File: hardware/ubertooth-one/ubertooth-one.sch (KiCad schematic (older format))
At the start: 88 parts, among them J1 USB-DEVICE, P1 SMA-CONN, P10 ATEST1, P11 ATEST2, P12 DCLK, P13 DIO, P2 PROGRAM, P3 JTAG, P4 EXPAND, P5 1V8, P6 3V3, P7 VBUS, P8 GIO1, P9 GIO6, Q1 BC856, U1 CC2591, U3 CC2400, U4 LPC175X, U6 IP4220CZ6, U7 TPS71219, X1 ABMM2

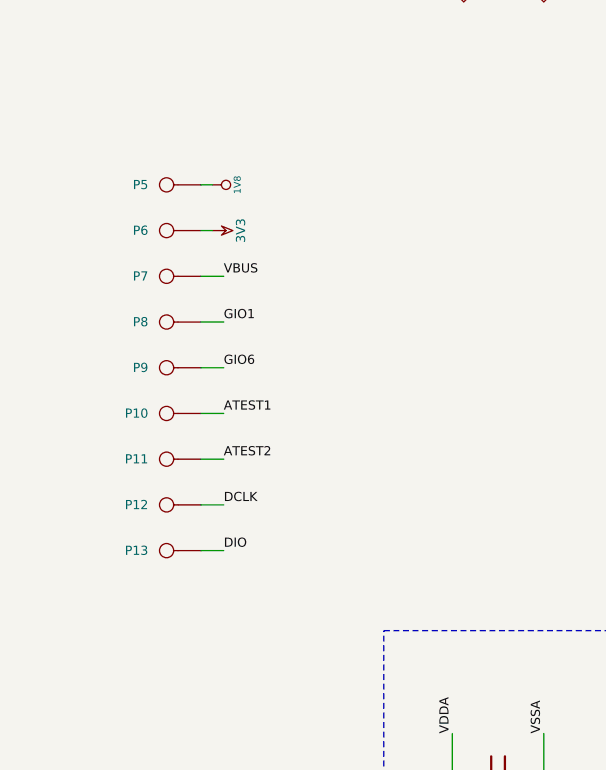
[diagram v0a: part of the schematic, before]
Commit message: added DNP fields
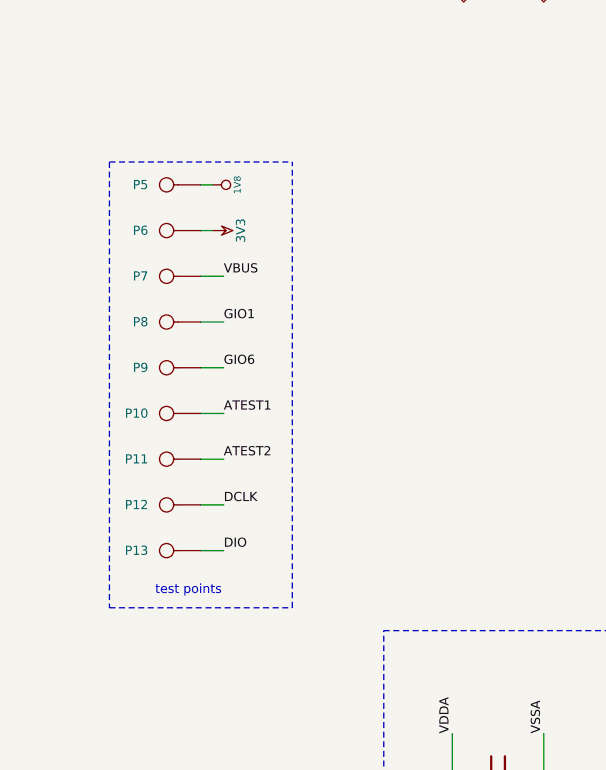
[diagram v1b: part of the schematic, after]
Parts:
- C10, C11, C8, FB1, FB2, FB3, FB4, L3, P2, P3, P4: Field3 (none) -> DNP
- C19, C21: footprint 0402 -> 0603
- C7: Field1 (none) -> foo; Field3 (none) -> DNP
- J1: footprint USB-A-MOLEX-480371000 -> USB-A-USAM-04
- P10, P11, P12, P13, P5, P6, P7, P8, P9: footprint (none) -> testpad-30mil; Field3 (none) -> DNP
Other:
- note added: "test points"

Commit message: rearranged regulator section with 0603s for ease of assembly
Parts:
- C35, C36, R18, R19: footprint 0402 -> 0603
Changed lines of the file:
@@
-EESchema Schematic File Version 2  date Sun Mar 20 08:07:46 2011
+EESchema Schematic File Version 2  date Sun Mar 20 10:47:56 2011
 LIBS:ubertooth-symbols
 LIBS:power
@@
 F 0 "C36" H 7250 7700 50  0000 L CNN
 F 1 "15pF" H 7250 7500 50  0000 L CNN
-F 2 "0402" H 7200 7600 60  0001 C CNN
+F 2 "0603" H 7200 7600 60  0001 C CNN
 F 4 "Murata" H 7200 7600 60  0001 C CNN "Field1"
 F 5 "GRM1535C1H150JDD5D" H 7200 7600 60  0001 C CNN "Field2"
@@
 F 0 "C35" H 6600 7750 50  0000 L CNN
 F 1 "10nF" H 6600 7550 50  0000 L CNN
-F 2 "0402" H 6550 7650 60  0001 C CNN
+F 2 "0603" H 6550 7650 60  0001 C CNN
 F 4 "Murata" H 6550 7650 60  0001 C CNN "Field1"
 F 5 "GRM155R71E103KA01D" H 6550 7650 60  0001 C CNN "Field2"
@@
 F 0 "R19" V 7030 8250 50  0000 C CNN
 F 1 "30.1k" V 6950 8250 50  0000 C CNN
-F 2 "0402" H 6950 8250 60  0001 C CNN
+F 2 "0603" H 6950 8250 60  0001 C CNN
 F 4 "KOA Speer" H 6950 8250 60  0001 C CNN "Field1"
 F 5 "RK73H1ETTP3012F" H 6950 8250 60  0001 C CNN "Field2"
@@
 F 0 "R18" V 7030 7550 50  0000 C CNN
 F 1 "49.9k" V 6950 7550 50  0000 C CNN
-F 2 "0402" H 6950 7550 60  0001 C CNN
+F 2 "0603" H 6950 7550 60  0001 C CNN
 F 4 "KOA Speer" H 6950 7550 60  0001 C CNN "Field1"
 F 5 "RK73H1ETTP4992F" H 6950 7550 60  0001 C CNN "Field2"

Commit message: bigger test pads
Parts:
- P10, P11, P12, P13, P5, P6, P7, P8, P9: footprint testpad-30mil -> testpad-50mil
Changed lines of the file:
@@
-EESchema Schematic File Version 2  date Sun Mar 20 10:47:56 2011
+EESchema Schematic File Version 2  date Sun Mar 20 21:47:07 2011
 LIBS:ubertooth-symbols
 LIBS:power
@@
 F 0 "P13" H 1280 7550 40  0000 L CNN
 F 1 "DIO" H 1200 7605 30  0001 C CNN
-F 2 "testpad-30mil" H 1200 7550 60  0001 C CNN
+F 2 "testpad-50mil" H 1200 7550 60  0001 C CNN
 F 4 "DNP" H 1200 7550 60  0001 C CNN "Field3"
 	1    1200 7550
@@
 F 0 "P12" H 1280 7350 40  0000 L CNN
 F 1 "DCLK" H 1200 7405 30  0001 C CNN
-F 2 "testpad-30mil" H 1200 7350 60  0001 C CNN
+F 2 "testpad-50mil" H 1200 7350 60  0001 C CNN
 F 4 "DNP" H 1200 7350 60  0001 C CNN "Field3"
 	1    1200 7350
@@
 F 0 "P9" H 1280 6750 40  0000 L CNN
 F 1 "GIO6" H 1200 6805 30  0001 C CNN
-F 2 "testpad-30mil" H 1200 6750 60  0001 C CNN
+F 2 "testpad-50mil" H 1200 6750 60  0001 C CNN
 F 4 "DNP" H 1200 6750 60  0001 C CNN "Field3"
 	1    1200 6750
@@
 F 0 "P11" H 1280 7150 40  0000 L CNN
 F 1 "ATEST2" H 1200 7205 30  0001 C CNN
-F 2 "testpad-30mil" H 1200 7150 60  0001 C CNN
+F 2 "testpad-50mil" H 1200 7150 60  0001 C CNN
 F 4 "DNP" H 1200 7150 60  0001 C CNN "Field3"
 	1    1200 7150
@@
 F 0 "P10" H 1280 6950 40  0000 L CNN
 F 1 "ATEST1" H 1200 7005 30  0001 C CNN
-F 2 "testpad-30mil" H 1200 6950 60  0001 C CNN
+F 2 "testpad-50mil" H 1200 6950 60  0001 C CNN
 F 4 "DNP" H 1200 6950 60  0001 C CNN "Field3"
 	1    1200 6950
@@
 F 0 "P8" H 1280 6550 40  0000 L CNN
 F 1 "GIO1" H 1200 6605 30  0001 C CNN
-F 2 "testpad-30mil" H 1200 6550 60  0001 C CNN
+F 2 "testpad-50mil" H 1200 6550 60  0001 C CNN
 F 4 "DNP" H 1200 6550 60  0001 C CNN "Field3"
 	1    1200 6550
@@
 F 0 "P7" H 1280 6350 40  0000 L CNN
 F 1 "VBUS" H 1200 6405 30  0001 C CNN
-F 2 "testpad-30mil" H 1200 6350 60  0001 C CNN
+F 2 "testpad-50mil" H 1200 6350 60  0001 C CNN
 F 4 "DNP" H 1200 6350 60  0001 C CNN "Field3"
 	1    1200 6350
@@
 F 0 "P6" H 1280 6150 40  0000 L CNN
 F 1 "3V3" H 1200 6205 30  0001 C CNN
-F 2 "testpad-30mil" H 1200 6150 60  0001 C CNN
+F 2 "testpad-50mil" H 1200 6150 60  0001 C CNN
 F 4 "DNP" H 1200 6150 60  0001 C CNN "Field3"
 	1    1200 6150
@@
 F 0 "P5" H 1280 5950 40  0000 L CNN
 F 1 "1V8" H 1200 6005 30  0001 C CNN
-F 2 "testpad-30mil" H 1200 5950 60  0001 C CNN
+F 2 "testpad-50mil" H 1200 5950 60  0001 C CNN
 F 4 "DNP" H 1200 5950 60  0001 C CNN "Field3"
 	1    1200 5950

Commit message: separated digital and analog 3V3
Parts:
- added FB5: FILTER, 0603, symbol FILTER
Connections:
- net 3V3: now also FB5.2; no longer C26.2, C27.1, C28.1, C30.2, C33.1, C34.1, D6.1 (A), FB1.2, FB3.2, P3.1, Q1.2 (E), R10.2, R14.2, R9.1, U4.16 (VBAT), U4.21 (VDD(3V3)), U4.34 (VDD(REG)(3V3)), U4.42 (VDD(3V3)), U4.56 (VDD(3V3)), U4.67 (VDD(REG)(3V3)), U4.77 (VDD(3V3))
- new net 3V3D: C26.2, C27.1, C28.1, C30.2, C33.1, C34.1, D6.1 (A), FB1.2, FB3.2, FB5.1, P3.1, Q1.2 (E), R10.2, R14.2, R9.1, U4.16 (VBAT), U4.21 (VDD(3V3)), U4.34 (VDD(REG)(3V3)), U4.42 (VDD(3V3)), U4.56 (VDD(3V3)), U4.67 (VDD(REG)(3V3)), U4.77 (VDD(3V3))

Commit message: bom update
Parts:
- C35: Field2 GRM155R71E103KA01D -> GRM188R71H103KA01D; Field3 Multilayer Ceramic Capacitors (MLCC) - SMD/SMT 0402 0.01uF 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 -> Multilayer Ceramic Capacitors (MLCC) - SMD/SMT 0603 0.01uF 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
- C36: Field2 GRM1535C1H150JDD5D -> GRM1885C1H150JA01D; Field3 Multilayer Ceramic Capacitors (MLCC) - SMD/SMT 0402 15pF 50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 -> Multilayer Ceramic Capacitors (MLCC) - SMD/SMT 0603 15pF 50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
- C7: Field1 foo -> (none)
- FB5: Field1 (none) -> Murata; Field2 (none) -> BLM18TG601TN1D; Field3 (none) -> EMI/RFI Suppressors & Ferrites 600 Ohm 25%
- R18: Field1 KOA Speer -> Panasonic; Field2 RK73H1ETTP4992F -> ERJ-3EKF4992V; Field3 Thick Film Resistors - SMD 0402 1/16watts 49.9Kohms -> Thick Film Resistors - SMD Thick Film Chip Res 0603 1% Prec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
- R19: Field1 KOA Speer -> Panasonic; Field2 RK73H1ETTP3012F -> ERJ-3EKF3012V; Field3 Thick Film Resistors - SMD 0402 1/16watts 30.1Kohms 1% -> Thick Film Resistors - SMD Thick Film Chip Res 0603 1% Prec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
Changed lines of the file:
@@
-EESchema Schematic File Version 2  date Sun Mar 20 22:13:36 2011
+EESchema Schematic File Version 2  date Fri Apr  1 21:17:36 2011
 LIBS:ubertooth-symbols
 LIBS:power
@@
 Sheet 1 1
 Title "Ubertooth One"
-Date "21 mar 2011"
+Date "2 apr 2011"
 Rev "$Rev$"
 Comp "Copyright 2010, 2011 Michael Ossmann"
@@
 F 1 "FILTER" H 5300 6300 60  0000 C CNN
 F 2 "0603" H 5300 6400 60  0001 C CNN
+F 4 "Murata" H 5300 6400 60  0001 C CNN "Field1"
+F 5 "BLM18TG601TN1D" H 5300 6400 60  0001 C CNN "Field2"
+F 6 "EMI/RFI Suppressors & Ferrites 600 Ohm 25%" H 5300 6400 60  0001 C CNN "Field3"
 	1    5300 6400
 	-1   0    0    1
@@
 F 2 "0603" H 7200 7600 60  0001 C CNN
 F 4 "Murata" H 7200 7600 60  0001 C CNN "Field1"
-F 5 "GRM1535C1H150JDD5D" H 7200 7600 60  0001 C CNN "Field2"
-F 6 "Multilayer Ceramic Capacitors (MLCC) - SMD/SMT 0402 15pF 50 volts 5%" H 7200 7600 60  0001 C CNN "Field3"
+F 5 "GRM1885C1H150JA01D" H 7200 7600 60  0001 C CNN "Field2"
+F 6 "Multilayer Ceramic Capacitors (MLCC) - SMD/SMT 0603 15pF 50volts C0G 5%" H 7200 7600 60  0001 C CNN "Field3"
 	1    7200 7600
 	1    0    0    -1
@@
 F 2 "0603" H 6550 7650 60  0001 C CNN
 F 4 "Murata" H 6550 7650 60  0001 C CNN "Field1"
-F 5 "GRM155R71E103KA01D" H 6550 7650 60  0001 C CNN "Field2"
-F 6 "Multilayer Ceramic Capacitors (MLCC) - SMD/SMT 0402 0.01uF 25volts X7R 10%" H 6550 7650 60  0001 C CNN "Field3"
+F 5 "GRM188R71H103KA01D" H 6550 7650 60  0001 C CNN "Field2"
+F 6 "Multilayer Ceramic Capacitors (MLCC) - SMD/SMT 0603 0.01uF 50volts X7R 10%" H 6550 7650 60  0001 C CNN "Field3"
 	1    6550 7650
 	1    0    0    -1
@@
 F 1 "30.1k" V 6950 8250 50  0000 C CNN
 F 2 "0603" H 6950 8250 60  0001 C CNN
-F 4 "KOA Speer" H 6950 8250 60  0001 C CNN "Field1"
-F 5 "RK73H1ETTP3012F" H 6950 8250 60  0001 C CNN "Field2"
-F 6 "Thick Film Resistors - SMD 0402 1/16watts 30.1Kohms 1%" H 6950 8250 60  0001 C CNN "Field3"
+F 4 "Panasonic" H 6950 8250 60  0001 C CNN "Field1"
+F 5 "ERJ-3EKF3012V" H 6950 8250 60  0001 C CNN "Field2"
+F 6 "Thick Film Resistors - SMD Thick Film Chip Res 0603 1% Precision" H 6950 8250 60  0001 C CNN "Field3"
 	1    6950 8250
 	1    0    0    -1
@@
 F 1 "49.9k" V 6950 7550 50  0000 C CNN
 F 2 "0603" H 6950 7550 60  0001 C CNN
-F 4 "KOA Speer" H 6950 7550 60  0001 C CNN "Field1"
-F 5 "RK73H1ETTP4992F" H 6950 7550 60  0001 C CNN "Field2"
-F 6 "Thick Film Resistors - SMD 0402 1/16watts 49.9Kohms" H 6950 7550 60  0001 C CNN "Field3"
+F 4 "Panasonic" H 6950 7550 60  0001 C CNN "Field1"
+F 5 "ERJ-3EKF4992V" H 6950 7550 60  0001 C CNN "Field2"
+F 6 "Thick Film Resistors - SMD Thick Film Chip Res 0603 1% Precision" H 6950 7550 60  0001 C CNN "Field3"
 	1    6950 7550
 	1    0    0    -1
@@
 F 2 "0603" H 2650 8550 60  0001 C CNN
 F 4 "DNP" H 2650 8550 60  0001 C CNN "Field3"
-F 5 "foo" H 2650 8550 60  0001 C CNN "Field1"
 	1    2650 8550
 	0    1    1    0

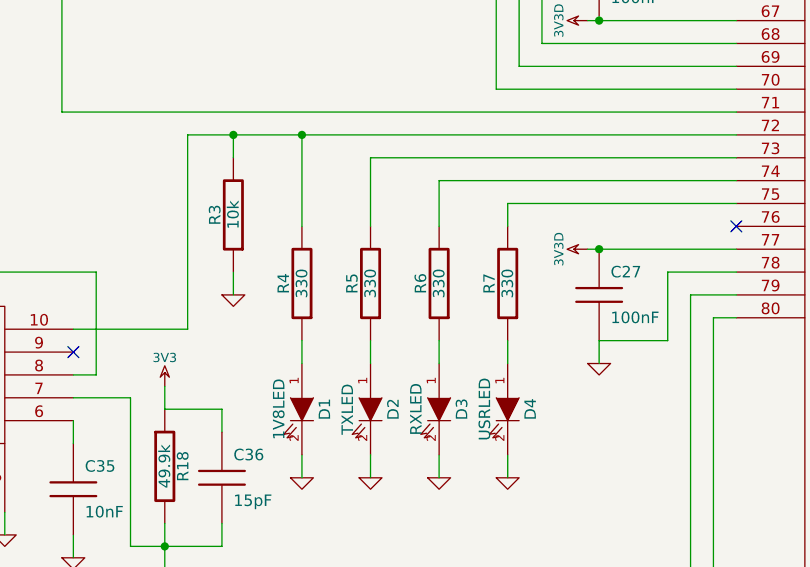
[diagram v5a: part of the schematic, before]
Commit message: changed series resistor values to even LED brightness
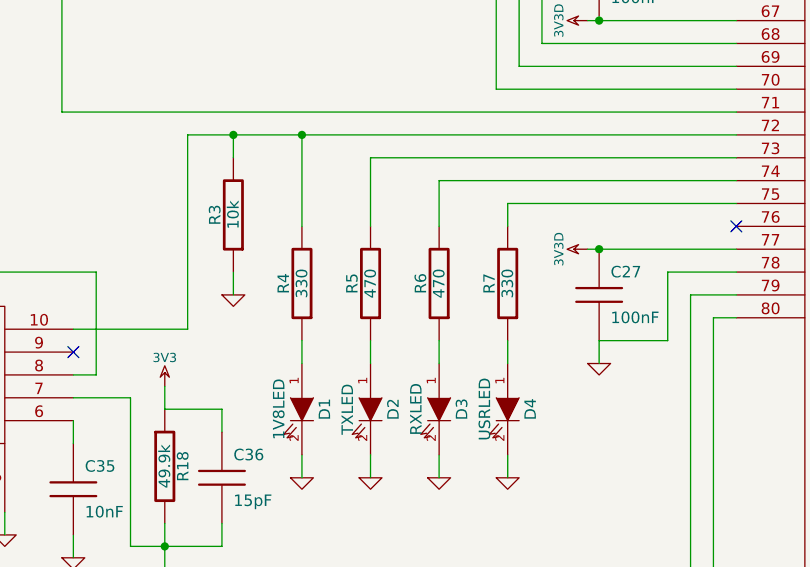
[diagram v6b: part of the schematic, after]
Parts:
- R5, R6: value 330 -> 470; Field2 CR0603-JW-331ELF -> CR0603-JW-471ELF; Field3 Thick Film Resistors - SMD 0603 330OHMS 5% 1/10WATT -> Thick Film Resistors - SMD 0603 470OHMS 5% 1/10WATT
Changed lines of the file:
@@
-EESchema Schematic File Version 2  date Fri Apr  1 21:17:36 2011
+EESchema Schematic File Version 2  date Thu Apr 21 15:42:57 2011
 LIBS:ubertooth-symbols
 LIBS:power
@@
 Sheet 1 1
 Title "Ubertooth One"
-Date "2 apr 2011"
+Date "21 apr 2011"
 Rev "$Rev$"
 Comp "Copyright 2010, 2011 Michael Ossmann"
@@
 P 7850 6750
 F 0 "R5" V 7930 6750 50  0000 C CNN
-F 1 "330" V 7850 6750 50  0000 C CNN
+F 1 "470" V 7850 6750 50  0000 C CNN
 F 2 "0603" H 7850 6750 60  0001 C CNN
 F 4 "Bourns" H 7850 6750 60  0001 C CNN "Field1"
-F 5 "CR0603-JW-331ELF" H 7850 6750 60  0001 C CNN "Field2"
-F 6 "Thick Film Resistors - SMD 0603 330OHMS 5% 1/10WATT" H 7850 6750 60  0001 C CNN "Field3"
+F 5 "CR0603-JW-471ELF" H 7850 6750 60  0001 C CNN "Field2"
+F 6 "Thick Film Resistors - SMD 0603 470OHMS 5% 1/10WATT" H 7850 6750 60  0001 C CNN "Field3"
 	1    7850 6750
 	-1   0    0    1
@@
 P 8150 6750
 F 0 "R6" V 8230 6750 50  0000 C CNN
-F 1 "330" V 8150 6750 50  0000 C CNN
+F 1 "470" V 8150 6750 50  0000 C CNN
 F 2 "0603" H 8150 6750 60  0001 C CNN
 F 4 "Bourns" H 8150 6750 60  0001 C CNN "Field1"
-F 5 "CR0603-JW-331ELF" H 8150 6750 60  0001 C CNN "Field2"
-F 6 "Thick Film Resistors - SMD 0603 330OHMS 5% 1/10WATT" H 8150 6750 60  0001 C CNN "Field3"
+F 5 "CR0603-JW-471ELF" H 8150 6750 60  0001 C CNN "Field2"
+F 6 "Thick Film Resistors - SMD 0603 470OHMS 5% 1/10WATT" H 8150 6750 60  0001 C CNN "Field3"
 	1    8150 6750
 	-1   0    0    1
